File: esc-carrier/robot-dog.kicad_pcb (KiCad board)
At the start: 2 copper layers, 74.3 x 78.1 mm, 38 parts, among them J1 Conn_01x02, J10 Conn_01x02, J11 Conn_01x04, J12 Conn_01x04, J13 Conn_01x04, J2 Conn_01x04, J3 Conn_01x04, J4 Conn_01x03, J5 Conn_01x05, J6 Conn_01x05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

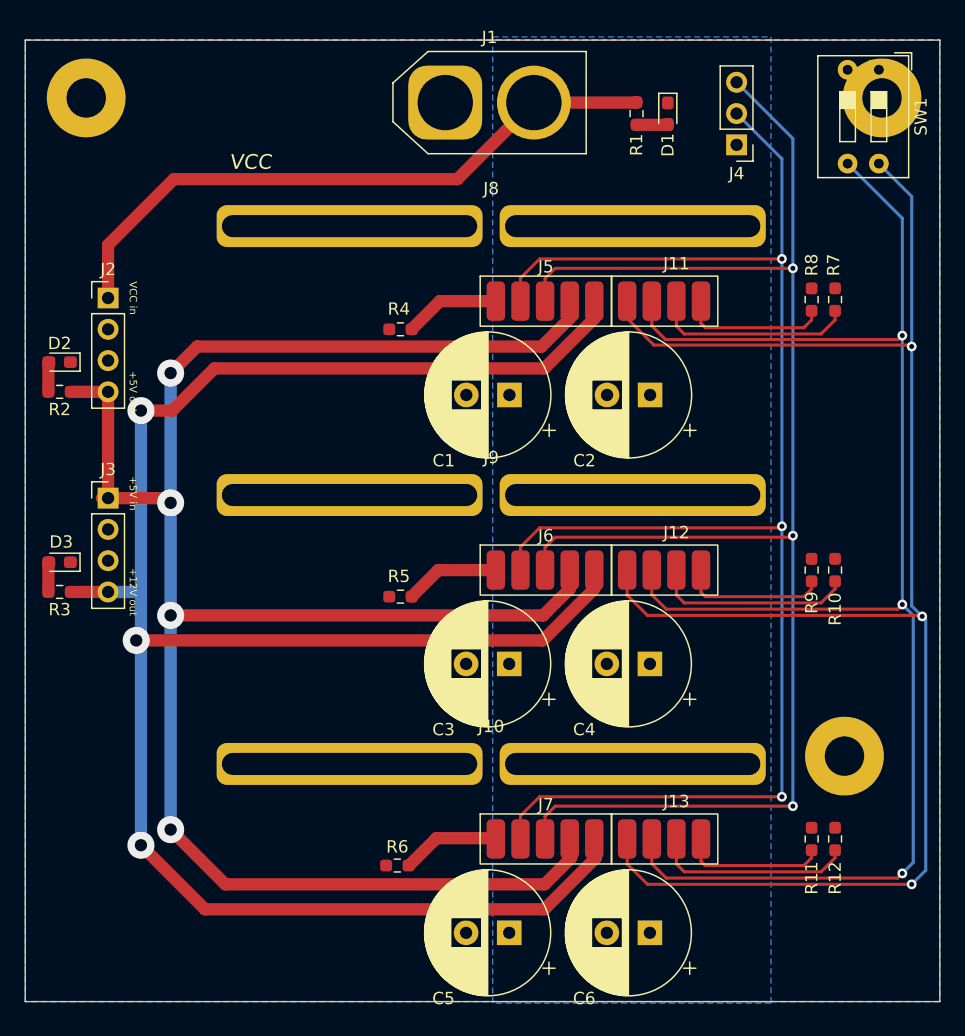
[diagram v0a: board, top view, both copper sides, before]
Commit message: reroute i2c
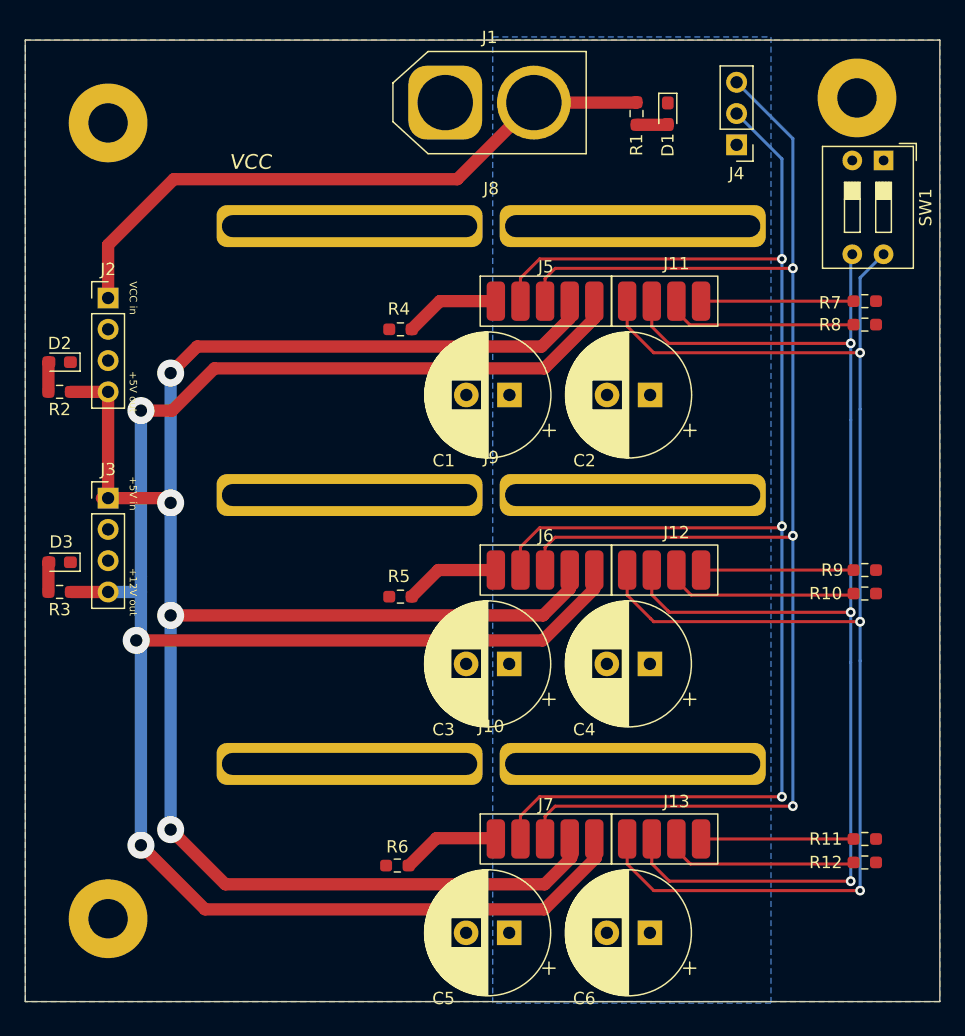
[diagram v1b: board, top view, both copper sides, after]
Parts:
- moved REF** 61.3 mm to (136.7, 107.4)
- moved SW1 7.38 mm to (199.6, 45.8)
- moved R8 4.77 mm to (198.1, 59.2), turned to 0 degrees
- moved R11 4.32 mm to (198.1, 101.0), turned to 0 degrees
- moved R9 4.32 mm to (198.1, 79.1), turned to 0 degrees
- moved R10 3.07 mm to (198.1, 81.0), turned to 0 degrees
- moved R12 3.07 mm to (198.1, 102.9), turned to 0 degrees
- moved REF** 2.70 mm to (136.7, 42.8)
- moved R7 2.42 mm to (198.1, 57.3), turned to 0 degrees
- moved REF** 2.03 mm to (197.5, 40.8)
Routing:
- net Net-(J11-Pad2): track 129.2 -> 107.3 mm
- net Net-(J11-Pad1): track 138.6 -> 118.0 mm
- net Net-(J11-Pad3): track 16.3 -> 15.7 mm
- net Net-(J13-Pad4): track 11.8 -> 12.4 mm
- net Net-(J11-Pad4): track 11.8 -> 12.4 mm
- net Net-(J12-Pad4): track 11.8 -> 12.4 mm
- net Net-(J12-Pad3): track 16.3 -> 15.8 mm

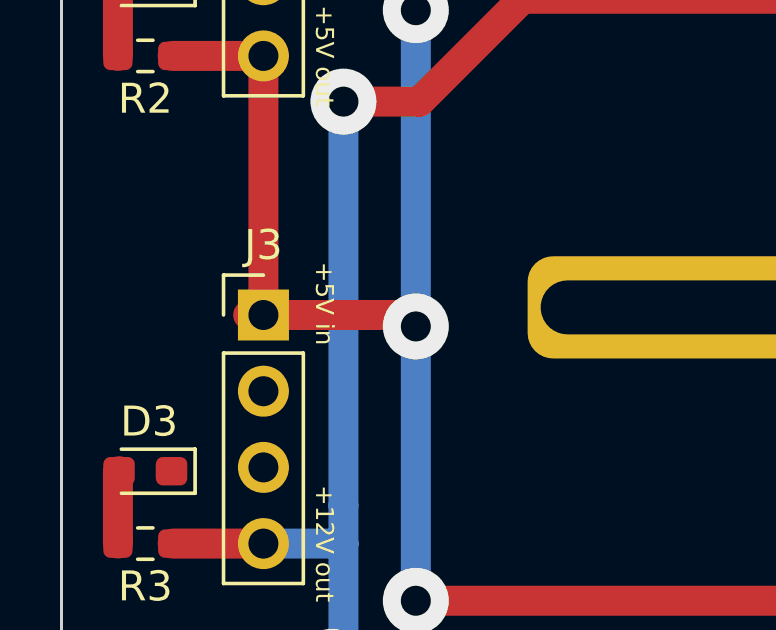
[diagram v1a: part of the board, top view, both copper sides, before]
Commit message: fix message 5v trace
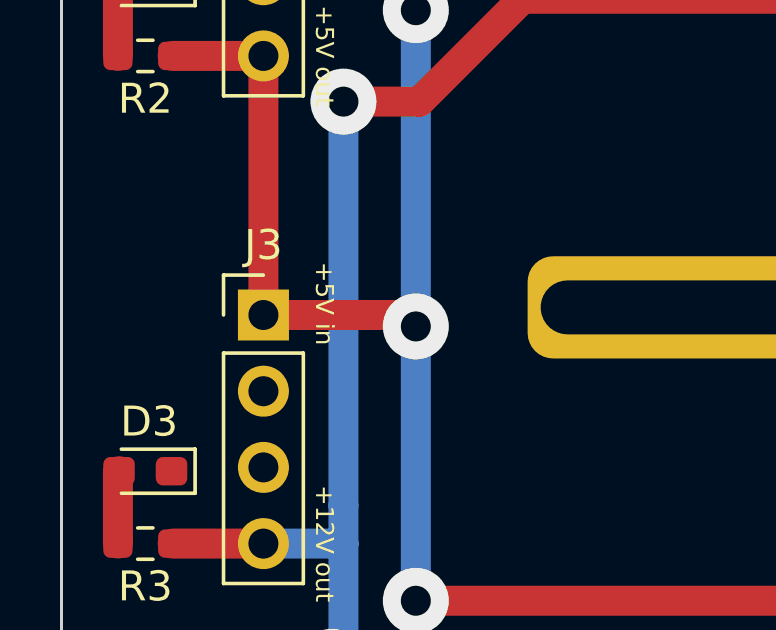
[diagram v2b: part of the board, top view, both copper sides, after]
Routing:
- net +5V: track 161.5 -> 161.0 mm
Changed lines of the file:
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@@
   (segment (start 131.8025 80.899) (end 131.8025 78.5235) (width 1) (layer "F.Cu") (net 5))
   (segment (start 131.8025 78.5235) (end 131.84 78.486) (width 1) (layer "F.Cu") (net 5))
-  (segment (start 141.351 73.279) (end 141.732 73.66) (width 1) (layer "F.Cu") (net 6))
   (segment (start 171.99 82.804) (end 141.732 82.804) (width 1) (layer "F.Cu") (net 6))
   (segment (start 174.149878 80.644122) (end 174.149878 79.241) (width 1) (layer "F.Cu") (net 6))
@@
   (segment (start 174.276878 102.488122) (end 172.117 104.648) (width 1) (layer "F.Cu") (net 6))
   (segment (start 174.148 57.276) (end 174.148 58.679122) (width 1) (layer "F.Cu") (net 6))
-  (segment (start 136.144 73.279) (end 141.351 73.279) (width 1) (layer "F.Cu") (net 6))
+  (segment (start 141.351 73.279) (end 141.732 73.66) (width 1) (layer "F.Cu") (net 6))
   (segment (start 146.177 104.648) (end 141.732 100.203) (width 1) (layer "F.Cu") (net 6))
   (segment (start 136.652 64.643) (end 136.652 73.279) (width 1) (layer "F.Cu") (net 6))
   (segment (start 174.148 58.679122) (end 171.864122 60.963) (width 1) (layer "F.Cu") (net 6))
+  (segment (start 136.652 73.279) (end 141.351 73.279) (width 1) (layer "F.Cu") (net 6))
   (segment (start 171.864122 60.963) (end 143.888 60.963) (width 1) (layer "F.Cu") (net 6))
   (via (at 141.732 100.203) (size 2.2) (drill 1) (layers "F.Cu" "B.Cu") (net 6))

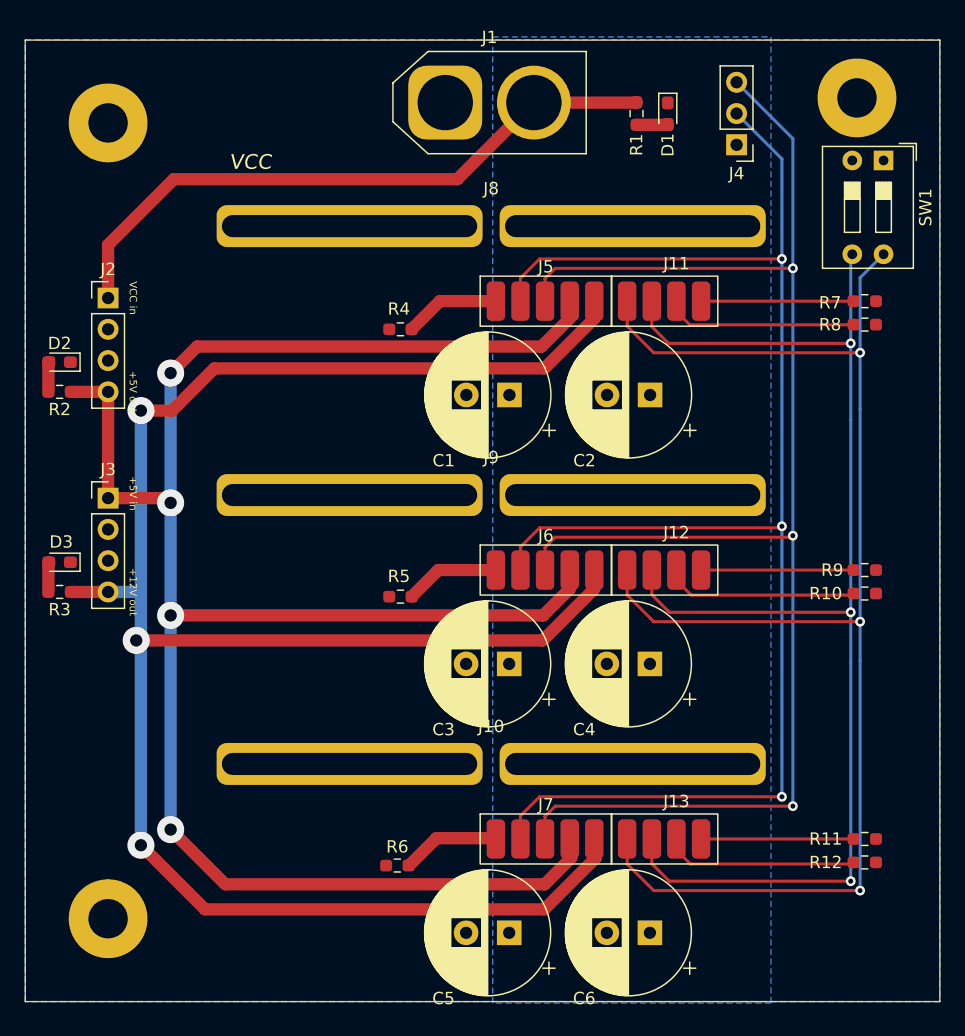
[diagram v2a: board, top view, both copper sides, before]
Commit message: edit silkscreen
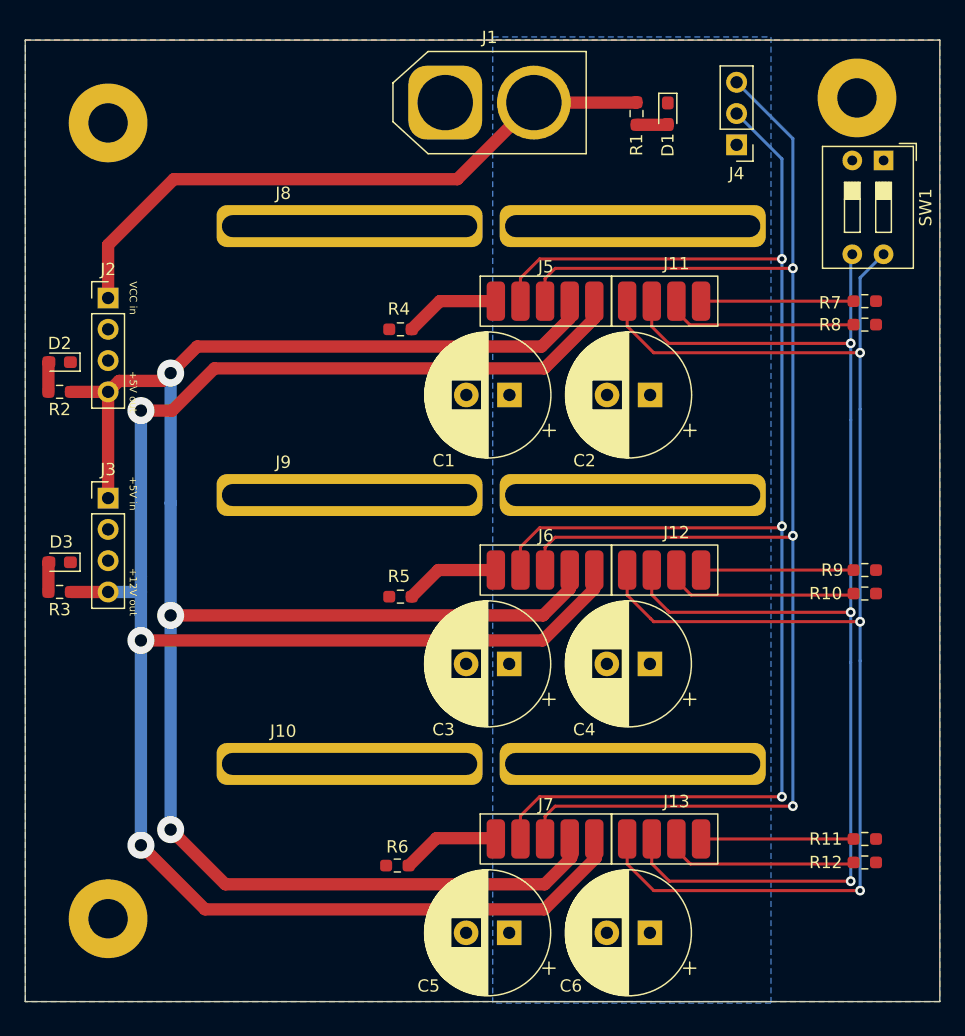
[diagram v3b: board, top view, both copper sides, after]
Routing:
- net +5V: track 161.0 -> 161.5 mm, vias 4 -> 3
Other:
- board text removed: "VCC"
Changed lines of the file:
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@@
     (property "Sheetname" "")
     (attr smd)
-    (fp_text reference "J10" (at 0 -3.048) (layer "F.SilkS")
+    (fp_text reference "J10" (at -16.891 -2.667) (layer "F.SilkS")
       (effects (font (size 1 1) (thickness 0.15)))
     )
@@
     (property "Sheetname" "")
     (attr through_hole)
-    (fp_text reference "C5" (at 5.334 -5.334) (layer "F.SilkS")
+    (fp_text reference "C5" (at 6.548 -4.318) (layer "F.SilkS")
       (effects (font (size 1 1) (thickness 0.15)))
     )
@@
     (property "Sheetname" "")
     (attr smd)
-    (fp_text reference "J8" (at 0 -3.048) (layer "F.SilkS")
+    (fp_text reference "J8" (at -16.891 -2.667) (layer "F.SilkS")
       (effects (font (size 1 1) (thickness 0.15)))
     )
@@
     (property "Sheetname" "")
     (attr smd)
-    (fp_text reference "J9" (at 0 -3.048) (layer "F.SilkS")
+    (fp_text reference "J9" (at -16.891 -2.667) (layer "F.SilkS")
       (effects (font (size 1 1) (thickness 0.15)))
     )
@@
     (property "Sheetname" "")
     (attr through_hole)
-    (fp_text reference "C6" (at 5.334 -5.334) (layer "F.SilkS")
+    (fp_text reference "C6" (at 6.421 -4.318) (layer "F.SilkS")
       (effects (font (size 1 1) (thickness 0.15)))
     )
@@
     (effects (font (size 0.6 0.6) (thickness 0.1)))
   )
-  (gr_text "VCC" (at 148.209 45.974) (layer "F.SilkS")
-    (effects (font (size 1.2 1.2) (thickness 0.2) italic))
-  )
   (dimension (type aligned) (layer "User.1")
     (pts (xy 197.485 40.767) (xy 204.216 40.767))
@@
   (segment (start 174.149878 80.644122) (end 174.149878 79.241) (width 1) (layer "F.Cu") (net 6))
   (segment (start 172.117 104.648) (end 146.177 104.648) (width 1) (layer "F.Cu") (net 6))
+  (segment (start 136.652 64.643) (end 137.541 63.754) (width 1) (layer "F.Cu") (net 6))
   (segment (start 171.99 82.804) (end 174.149878 80.644122) (width 1) (layer "F.Cu") (net 6))
   (segment (start 136.652 64.643) (end 133.6275 64.643) (width 1) (layer "F.Cu") (net 6))
@@
   (segment (start 174.276878 102.488122) (end 172.117 104.648) (width 1) (layer "F.Cu") (net 6))
   (segment (start 174.148 57.276) (end 174.148 58.679122) (width 1) (layer "F.Cu") (net 6))
-  (segment (start 141.351 73.279) (end 141.732 73.66) (width 1) (layer "F.Cu") (net 6))
   (segment (start 146.177 104.648) (end 141.732 100.203) (width 1) (layer "F.Cu") (net 6))
   (segment (start 136.652 64.643) (end 136.652 73.279) (width 1) (layer "F.Cu") (net 6))
   (segment (start 174.148 58.679122) (end 171.864122 60.963) (width 1) (layer "F.Cu") (net 6))
-  (segment (start 136.652 73.279) (end 141.351 73.279) (width 1) (layer "F.Cu") (net 6))
+  (segment (start 141.097 63.754) (end 141.732 63.119) (width 1) (layer "F.Cu") (net 6))
   (segment (start 171.864122 60.963) (end 143.888 60.963) (width 1) (layer "F.Cu") (net 6))
+  (segment (start 137.541 63.754) (end 141.097 63.754) (width 1) (layer "F.Cu") (net 6))
   (via (at 141.732 100.203) (size 2.2) (drill 1) (layers "F.Cu" "B.Cu") (net 6))
-  (via (at 141.732 73.66) (size 2.2) (drill 1) (layers "F.Cu" "B.Cu") (net 6))
   (via (at 141.732 82.804) (size 2.2) (drill 1) (layers "F.Cu" "B.Cu") (net 6))
   (via (at 141.732 63.119) (size 2.2) (drill 1) (layers "F.Cu" "B.Cu") (net 6))
   (segment (start 141.732 73.66) (end 141.732 63.119) (width 1) (layer "B.Cu") (net 6))
   (segment (start 141.732 100.203) (end 141.732 73.6925) (width 1) (layer "B.Cu") (net 6))
+  (segment (start 139.319 84.836) (end 171.958 84.836) (width 1) (layer "F.Cu") (net 7))
   (segment (start 176.276878 102.488122) (end 172.085 106.68) (width 1) (layer "F.Cu") (net 7))
   (segment (start 172.089122 62.738) (end 176.148 58.679122) (width 1) (layer "F.Cu") (net 7))
@@
   (segment (start 172.085 106.68) (end 144.526 106.68) (width 1) (layer "F.Cu") (net 7))
   (segment (start 139.319 66.167) (end 141.859 66.167) (width 1) (layer "F.Cu") (net 7))
+  (segment (start 176.149878 80.644122) (end 176.149878 79.241) (width 1) (layer "F.Cu") (net 7))
   (segment (start 144.526 106.68) (end 139.319 101.473) (width 1) (layer "F.Cu") (net 7))
-  (segment (start 176.149878 80.644122) (end 171.958 84.836) (width 1) (layer "F.Cu") (net 7))
+  (segment (start 171.958 84.836) (end 176.149878 80.644122) (width 1) (layer "F.Cu") (net 7))
   (segment (start 176.148 58.679122) (end 176.148 57.276) (width 1) (layer "F.Cu") (net 7))
   (segment (start 141.859 66.167) (end 145.288 62.738) (width 1) (layer "F.Cu") (net 7))
-  (segment (start 171.958 84.836) (end 138.938 84.836) (width 1) (layer "F.Cu") (net 7))
-  (segment (start 176.149878 79.241) (end 176.149878 80.644122) (width 1) (layer "F.Cu") (net 7))
   (via (at 139.319 66.167) (size 2.2) (drill 1) (layers "F.Cu" "B.Cu") (net 7))
-  (via (at 138.938 84.836) (size 2.2) (drill 1) (layers "F.Cu" "B.Cu") (net 7))
+  (via (at 139.319 84.836) (size 2.2) (drill 1) (layers "F.Cu" "B.Cu") (net 7))
   (via (at 139.319 101.473) (size 2.2) (drill 1) (layers "F.Cu" "B.Cu") (net 7))
   (segment (start 139.319 101.473) (end 139.319 80.899) (width 1) (layer "B.Cu") (net 7))
